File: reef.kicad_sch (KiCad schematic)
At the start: 60 parts, among them J1 T4140012051-000, J2 T4140012051-000, U1 nice_nano

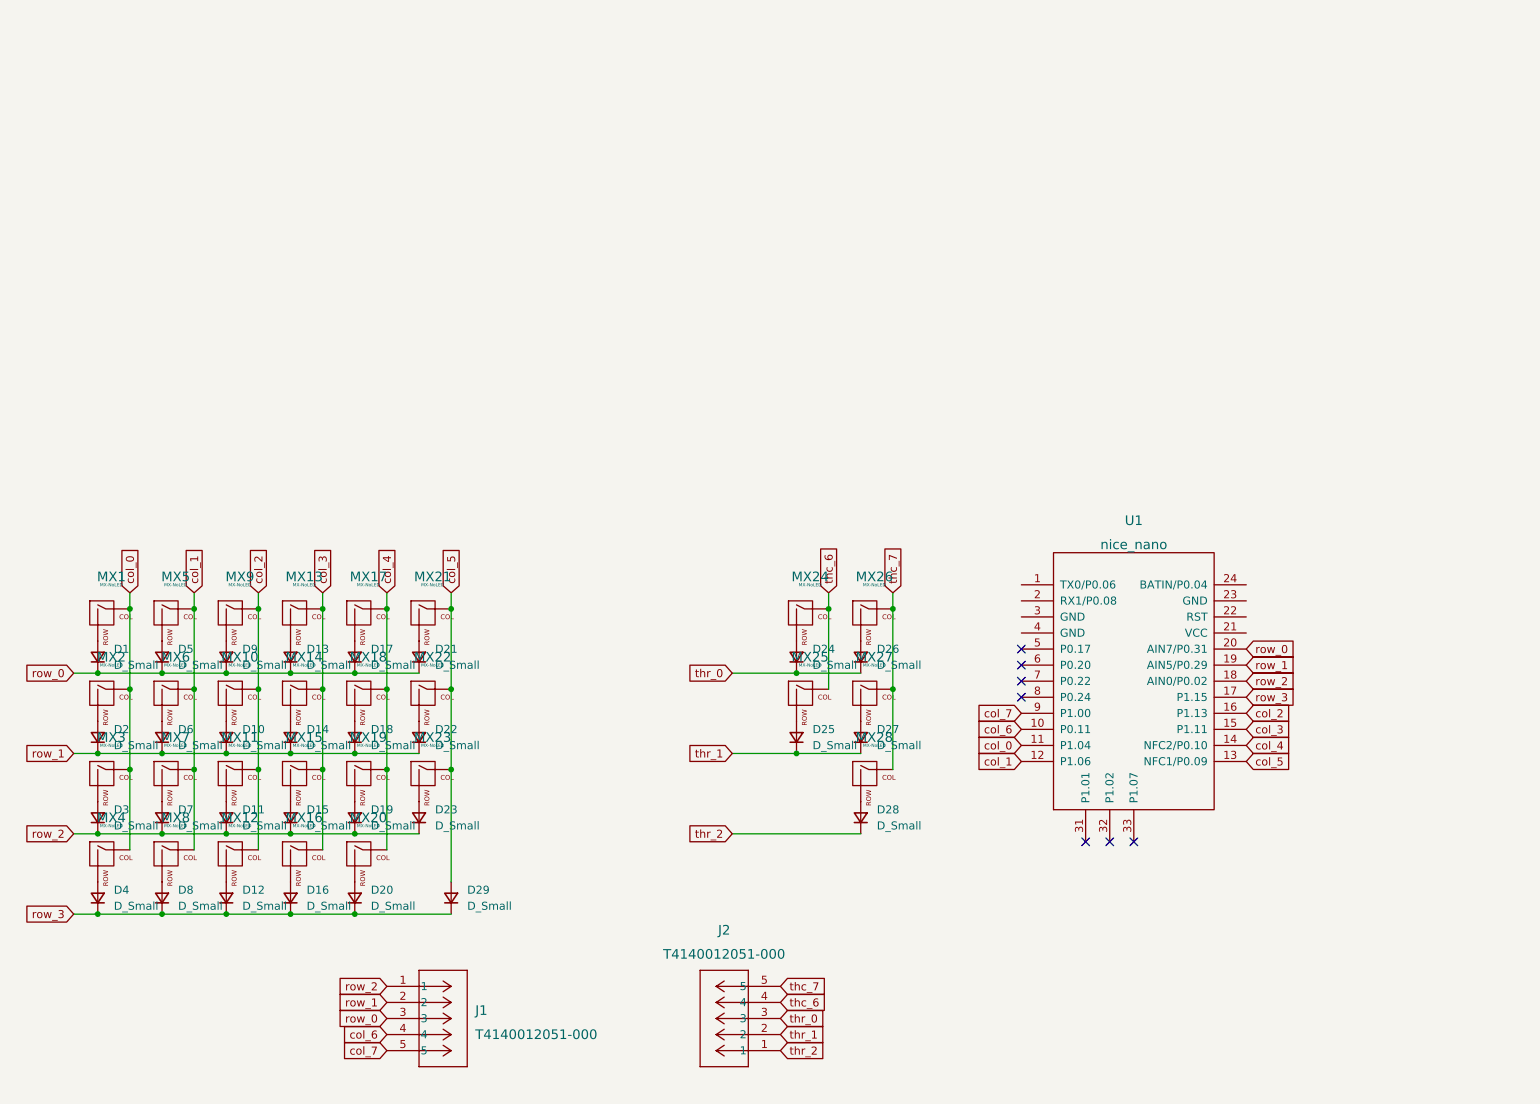
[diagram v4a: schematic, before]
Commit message: Updated Layout
modified layout to use trrs to connect with thumb cluster, added connector for battery, and footprint for nice!view display
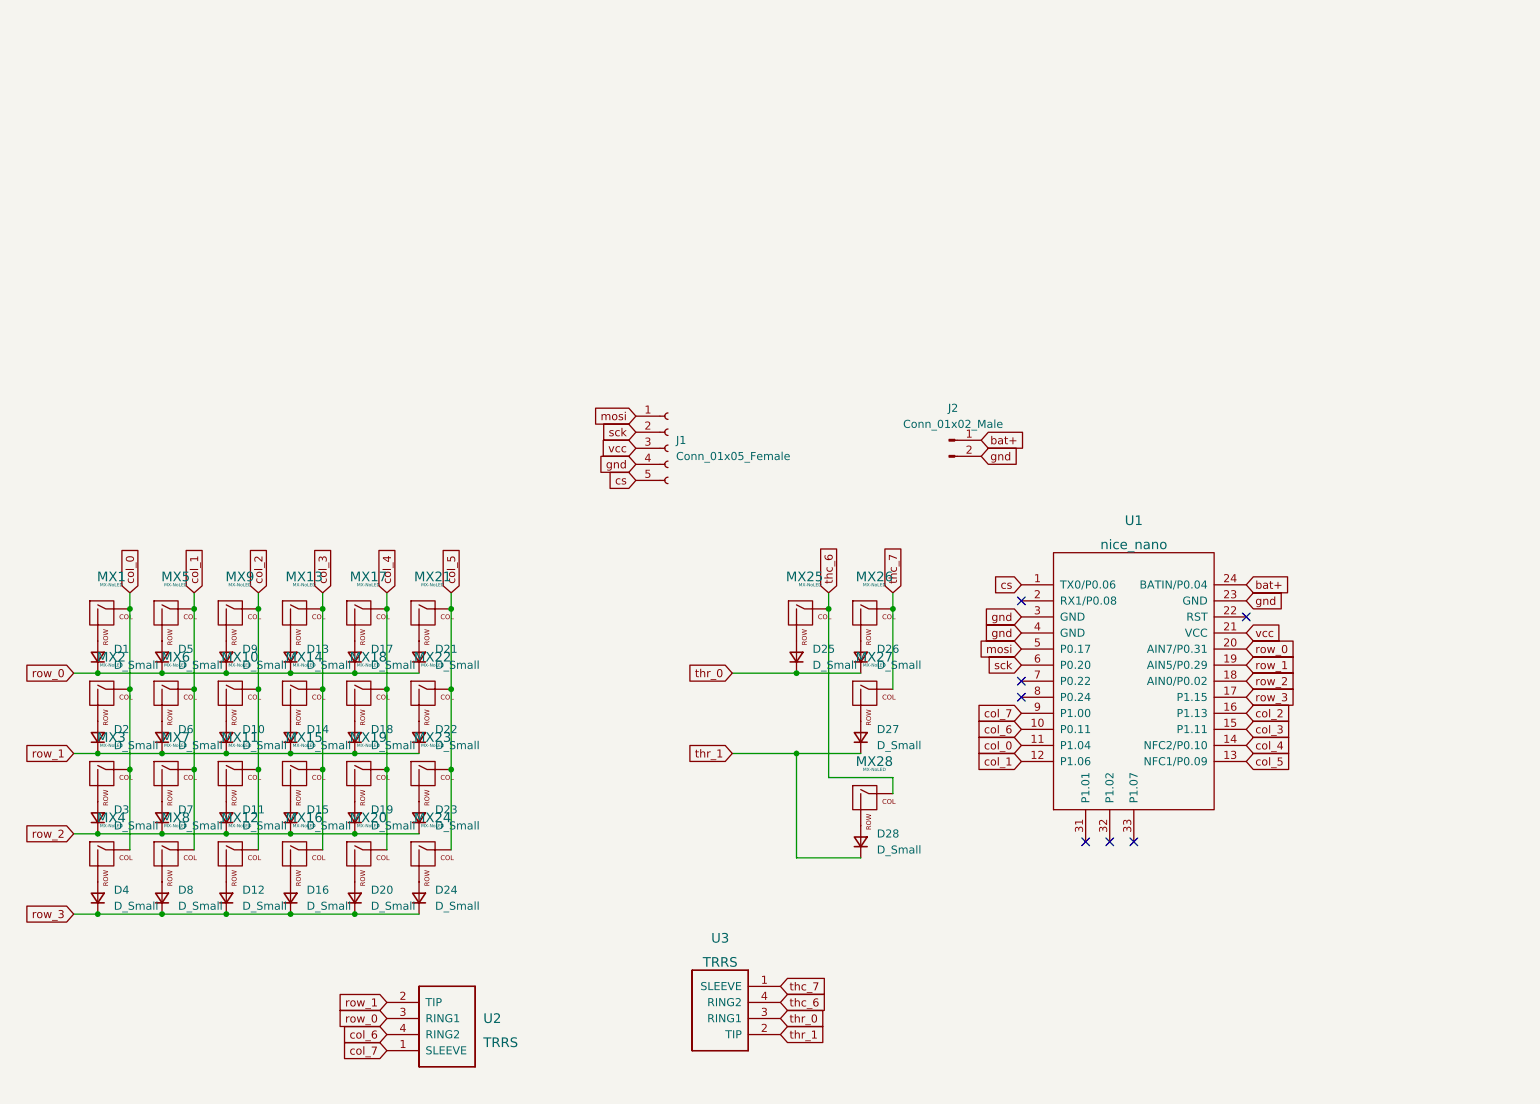
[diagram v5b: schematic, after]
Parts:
- removed D29: D_Small, modified_footprints:D_SOD-123_reversible, symbol Device:D_Small
- removed J1, J2: T4140012051-000, footprints:CONN5_T4140012051_TEC, symbol 2023-08-20_16-16-57:T4140012051-000
- added J1: Conn_01x05_Female, modified_footprints:nice_view_adapted, symbol Connector:Conn_01x05_Female
- added J2: Conn_01x02_Male, Connector_JST:JST_PH_S2B-PH-K_1x02_P2.00mm_Horizontal, symbol Connector:Conn_01x02_Male
- added U2, U3: TRRS, Keebio-Parts:TRRS-PJ-320A, symbol keebio:TRRS
- MX25: footprint MX_Only:MXOnly-2U-Hotswap -> MX_Only:MXOnly-2.25U-Hotswap
- MX26, MX27, MX28: footprint MX_Only:MXOnly-1.25U-Hotswap -> MX_Only:MXOnly-1.5U-Hotswap
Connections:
- net thr_2 is gone; now on net thr_1: D28.1 (K)
- net col_5: now also MX24.1 (COL)
- net col_6: now also U2.4 (RING2)
- net col_7: now also U2.1 (SLEEVE)
- net row_0: now also U2.3 (RING1)
- net row_1: now also U2.2 (TIP)
- net row_3: now also D24.1 (K)
- net thc_6: now also MX28.1 (COL), U3.4 (RING2); no longer MX24.1 (COL)
- net thc_7: now also U3.1 (SLEEVE); no longer MX28.1 (COL)
- net thr_0: now also D25.1 (K), U3.3 (RING1); no longer D24.1 (K)
- net thr_1: now also U3.2 (TIP); no longer D25.1 (K)
- net cs: now reaches U1.1 (TX0/P0.06)
- net cs: now also J1.5 (Pin_5)
- net vcc: now reaches U1.21 (VCC)
- net vcc: now also J1.3 (Pin_3)
- net gnd: now reaches U1.23 (GND)
- net gnd: now also U1.3 (GND), U1.4 (GND), J1.4 (Pin_4), J2.2 (Pin_2)
- net bat+: now reaches U1.24 (BATIN/P0.04)
- net bat+: now also J2.1 (Pin_1)
- net mosi: now reaches U1.5 (P0.17)
- net mosi: now also J1.1 (Pin_1)
- net sck: now reaches U1.6 (P0.20)
- net sck: now also J1.2 (Pin_2)
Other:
- moved on the sheet: D24, D25, D28, MX24, MX25, MX28

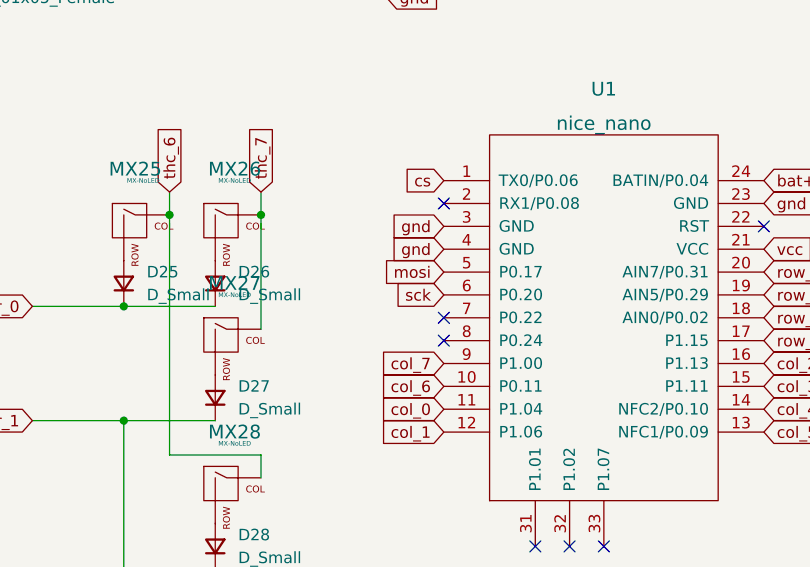
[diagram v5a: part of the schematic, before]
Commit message: Route Display
Display connected to nice!nano. in order to keep pcb reversible, jumper wire will be soldered between the actual display pad footprint and the appropriate column of pads (J1)
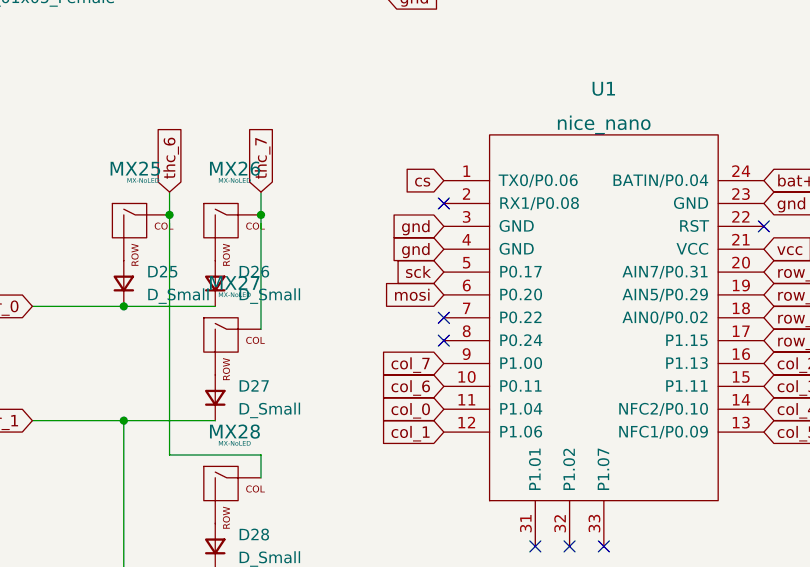
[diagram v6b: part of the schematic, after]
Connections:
- net mosi: now also U1.6 (P0.20); no longer U1.5 (P0.17)
- net sck: now also U1.5 (P0.17); no longer U1.6 (P0.20)
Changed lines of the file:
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@@
     )
   )
-  (global_label "mosi" (shape input) (at 185.42 120.65 180) (fields_autoplaced)
+  (global_label "mosi" (shape input) (at 185.42 123.19 180) (fields_autoplaced)
     (effects (font (size 1.27 1.27)) (justify right))
-    (property "Intersheet References" "${INTERSHEET_REFS}" (id 0) (at 178.5317 120.5706 0)
+    (property "Intersheet References" "${INTERSHEET_REFS}" (id 0) (at 178.5317 123.1106 0)
       (effects (font (size 1.27 1.27)) (justify right) hide)
     )
@@
     )
   )
-  (global_label "sck" (shape input) (at 185.42 123.19 180) (fields_autoplaced)
+  (global_label "sck" (shape input) (at 185.42 120.65 180) (fields_autoplaced)
     (effects (font (size 1.27 1.27)) (justify right))
-    (property "Intersheet References" "${INTERSHEET_REFS}" (id 0) (at 179.8621 123.1106 0)
+    (property "Intersheet References" "${INTERSHEET_REFS}" (id 0) (at 179.8621 120.5706 0)
       (effects (font (size 1.27 1.27)) (justify right) hide)
     )

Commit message: Reversible via Jumper Pads
using solder jumper pads to make component footprints reversible
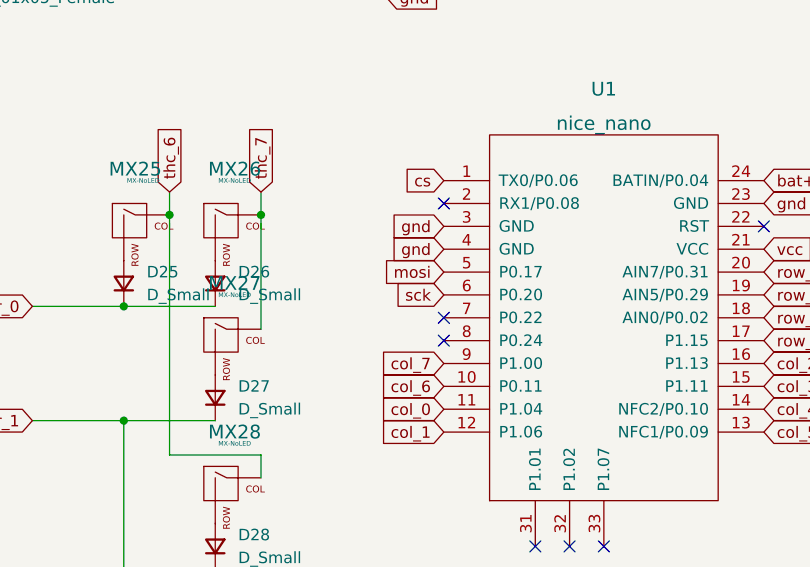
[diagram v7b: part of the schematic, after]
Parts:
- U1: footprint nice-nano-kicad:nice_nano -> keyboard_reversible:ProMicro
- U2, U3: footprint Keebio-Parts:TRRS-PJ-320A -> keyboard_reversible:PJ-320A
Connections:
- net mosi: now also U1.5 (P0.17); no longer U1.6 (P0.20)
- net sck: now also U1.6 (P0.20); no longer U1.5 (P0.17)
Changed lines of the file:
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@@
     )
   )
-  (global_label "mosi" (shape input) (at 185.42 123.19 180) (fields_autoplaced)
-    (effects (font (size 1.27 1.27)) (justify right))
-    (property "Intersheet References" "${INTERSHEET_REFS}" (id 0) (at 178.5317 123.1106 0)
+  (global_label "mosi" (shape input) (at 185.42 120.65 180) (fields_autoplaced)
+    (effects (font (size 1.27 1.27)) (justify right))
+    (property "Intersheet References" "${INTERSHEET_REFS}" (id 0) (at 178.5317 120.5706 0)
       (effects (font (size 1.27 1.27)) (justify right) hide)
     )
@@
     )
   )
-  (global_label "sck" (shape input) (at 185.42 120.65 180) (fields_autoplaced)
-    (effects (font (size 1.27 1.27)) (justify right))
-    (property "Intersheet References" "${INTERSHEET_REFS}" (id 0) (at 179.8621 120.5706 0)
+  (global_label "sck" (shape input) (at 185.42 123.19 180) (fields_autoplaced)
+    (effects (font (size 1.27 1.27)) (justify right))
+    (property "Intersheet References" "${INTERSHEET_REFS}" (id 0) (at 179.8621 123.1106 0)
       (effects (font (size 1.27 1.27)) (justify right) hide)
     )
@@
       (effects (font (size 1.524 1.524)))
     )
-    (property "Footprint" "nice-nano-kicad:nice_nano" (id 2) (at 229.87 187.96 90)
+    (property "Footprint" "keyboard_reversible:ProMicro" (id 2) (at 229.87 187.96 90)
       (effects (font (size 1.524 1.524)) hide)
     )
@@
       (effects (font (size 1.524 1.524)))
     )
-    (property "Footprint" "Keebio-Parts:TRRS-PJ-320A" (id 2) (at 134.62 171.45 0)
+    (property "Footprint" "keyboard_reversible:PJ-320A" (id 2) (at 134.62 171.45 0)
       (effects (font (size 1.524 1.524)) hide)
     )
@@
       (effects (font (size 1.524 1.524)) (justify left))
     )
-    (property "Footprint" "Keebio-Parts:TRRS-PJ-320A" (id 2) (at 97.79 186.69 0)
+    (property "Footprint" "keyboard_reversible:PJ-320A" (id 2) (at 97.79 186.69 0)
       (effects (font (size 1.524 1.524)) hide)
     )
@@
     )
     (path "/15da0337-5c17-4a0d-8eb2-6b931e23aa73"
-      (reference "U1") (unit 1) (value "nice_nano") (footprint "nice-nano-kicad:nice_nano")
+      (reference "U1") (unit 1) (value "nice_nano") (footprint "keyboard_reversible:ProMicro")
     )
     (path "/dda3e608-d82c-40cc-84d2-9f44284e00b8"
-      (reference "U2") (unit 1) (value "TRRS") (footprint "Keebio-Parts:TRRS-PJ-320A")
+      (reference "U2") (unit 1) (value "TRRS") (footprint "keyboard_reversible:PJ-320A")
     )
     (path "/89bb5d1e-f7e8-44dd-80d0-bfcb1a982e08"
-      (reference "U3") (unit 1) (value "TRRS") (footprint "Keebio-Parts:TRRS-PJ-320A")
-    )
-  )
+      (reference "U3") (unit 1) (value "TRRS") (footprint "keyboard_reversible:PJ-320A")
+    )
+  )

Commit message: Display Routing
Traces for display should no longer interfere with routing columns and rows to their respective pins in an aesthetically pleasing manner...hopefully
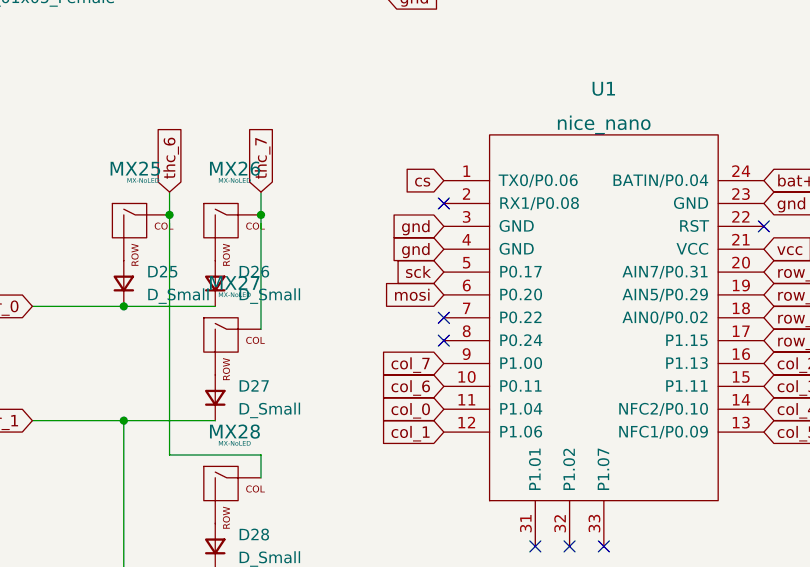
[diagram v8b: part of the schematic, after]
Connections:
- net mosi: now also U1.6 (P0.20); no longer U1.5 (P0.17)
- net sck: now also U1.5 (P0.17); no longer U1.6 (P0.20)
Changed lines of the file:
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@@
     )
   )
-  (global_label "mosi" (shape input) (at 185.42 120.65 180) (fields_autoplaced)
+  (global_label "mosi" (shape input) (at 185.42 123.19 180) (fields_autoplaced)
     (effects (font (size 1.27 1.27)) (justify right))
-    (property "Intersheet References" "${INTERSHEET_REFS}" (id 0) (at 178.5317 120.5706 0)
+    (property "Intersheet References" "${INTERSHEET_REFS}" (id 0) (at 178.5317 123.1106 0)
       (effects (font (size 1.27 1.27)) (justify right) hide)
     )
@@
     )
   )
-  (global_label "sck" (shape input) (at 185.42 123.19 180) (fields_autoplaced)
+  (global_label "sck" (shape input) (at 185.42 120.65 180) (fields_autoplaced)
     (effects (font (size 1.27 1.27)) (justify right))
-    (property "Intersheet References" "${INTERSHEET_REFS}" (id 0) (at 179.8621 123.1106 0)
+    (property "Intersheet References" "${INTERSHEET_REFS}" (id 0) (at 179.8621 120.5706 0)
       (effects (font (size 1.27 1.27)) (justify right) hide)
     )
